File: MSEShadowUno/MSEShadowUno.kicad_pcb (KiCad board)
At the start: 2 copper layers, 68.9 x 53.7 mm, 10 parts, among them J1 MDFly MP3 Trigger, J2 Power In, J3 Sparkfun MP3 Trigger, J4 Power Jumper, J5 Motor, J6 Servo, J7 Audio Out, U1 ATMEGA328P-PU

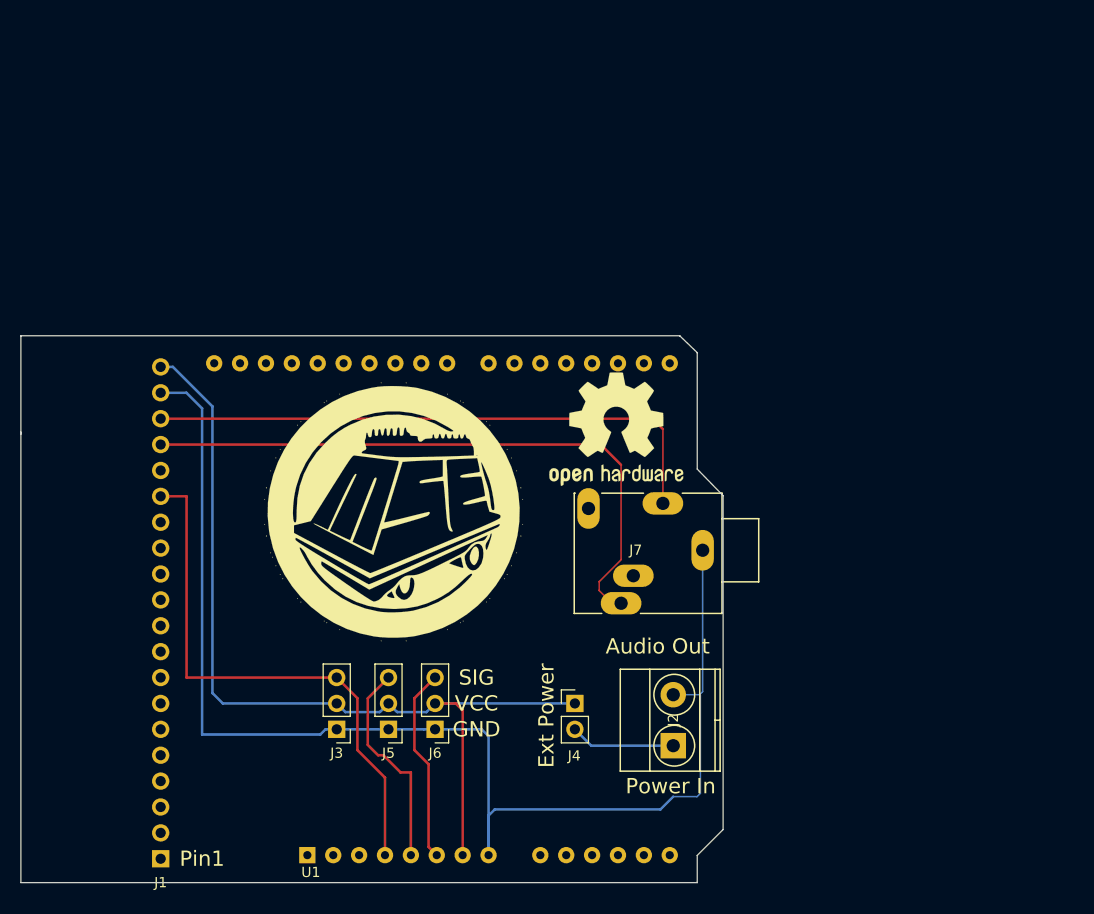
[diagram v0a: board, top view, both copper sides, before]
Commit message: Update PCB Board
Update PCB board to use Arduino Uno Shield instead of Atmel chip
(this fixes routing problems between the schematic and PCB)

Remove generated Gerber files
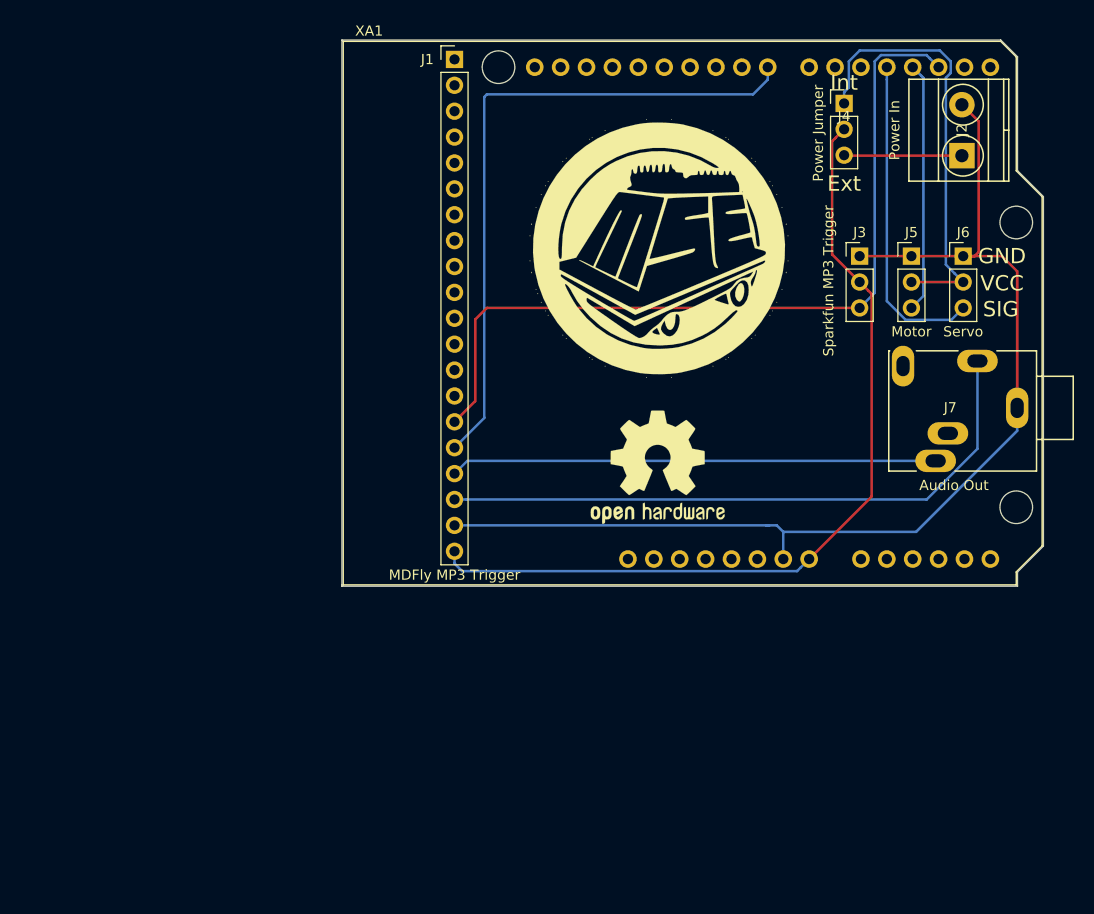
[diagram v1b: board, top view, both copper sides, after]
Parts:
- removed the G*** at (153.9, 98.2)
- removed U1: ATMEGA328P-PU, Modules:Arduino_UNO_R3
- added G***: LOGO, MSEShadowUno:MSE-NOText-Normal, F.Cu at (180.0, 72.4)
- added XA1: Arduino_Uno_Shield, Arduino:Arduino_Uno_Shield_No_ICSP, F.Cu at (149.0, 105.4)
- J1: moved to F.Cu
- J4: footprint Pin_Headers:Pin_Header_Straight_1x02_Pitch2.54mm -> Pin_Headers:Pin_Header_Straight_1x03_Pitch2.54mm
- moved J1 83.6 mm to (159.9, 53.8)
- moved J6 69.6 mm to (209.8, 73.2), turned to 0 degrees
- moved J3 69.2 mm to (199.6, 73.2), turned to 0 degrees
- moved J5 69.2 mm to (204.7, 73.2), turned to 0 degrees
- moved J4 64.5 mm to (198.1, 58.2)
- moved J2 64.4 mm to (209.7, 63.3)
- moved J7 33.9 mm to (211.2, 83.4)
- moved REF*** 5.52 mm to (179.8, 93.9)
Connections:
- J4 pad 1: Net-(J1-Pad20) -> Net-(J4-Pad1)
- J4 pad 2: Net-(J2-Pad1) -> Net-(J1-Pad20)
- J5 pad 2: Net-(J1-Pad20) -> Net-(J4-Pad1)
- J6 pad 2: Net-(J1-Pad20) -> Net-(J4-Pad1)
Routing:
- net Net-(J1-Pad16): track 0.00 -> 65.4 mm
- net Net-(J4-Pad1): track 0.00 -> 42.8 mm
- net Net-(J1-Pad15): track 54.4 -> 80.9 mm
- net Net-(J1-Pad19): track 129.1 -> 111.0 mm
- net Net-(J1-Pad17): track 63.3 -> 47.7 mm
- net Net-(J6-Pad3): track 19.2 -> 31.7 mm
- net Net-(J1-Pad20): track 89.4 -> 83.6 mm
- net Net-(J1-Pad18): track 57.0 -> 62.0 mm
- net Net-(J5-Pad3): track 20.9 -> 24.5 mm
- net Net-(J2-Pad1): track 10.3 -> 11.6 mm
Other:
- board size 68.9 x 53.7 mm -> 68.8 x 53.6 mm
- net class Default: clearance 0.1524 -> 0.2; trace_width 0.1524 -> 0.25; via_dia 0.6858 -> 0.6; via_drill 0.3302 -> 0.4
- rule trace_clearance: 0.1524 -> 0.2
- rule trace_min: 0.1524 -> 0.2
- rule via_min_drill: 0.254 -> 0.3
- rule via_min_size: 0.508 -> 0.4
- board text added: "Ext"
- board text added: "Int"
- board text removed: "Audio Out"
- board text removed: "Ext Power"
- board text removed: "Pin1"
- board text removed: "Power In"
